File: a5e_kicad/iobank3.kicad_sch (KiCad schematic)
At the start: 3 parts, among them U7 A5EB013B-B23B

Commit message: Add LCSC part numbers and fix C102 footprint
Add a hidden LCSC field to 290 symbols from the JLCPCB parts match
(2026-10-23). Left without LCSC: U7, U15, L1 (not in the JLCPCB
library), C1/C2/C4 and L2-L5 (no value specified), J3 (no confident
match) and Y3 (the 12 pF Basic crystal does not suit the 27 pF load
caps). U2, U12, Y2 and J9 carry the exact-MPN LCSC numbers although
they currently show zero JLCPCB stock.

C102 (22U 6V3) had a 0201 footprint; no 22 uF 0201 part exists. Change
it to 0402 (C415703) like C5-C7.
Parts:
- R23, R248: LCSC (none) -> C25094
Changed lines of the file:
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@@
+			)
+		)
+		(property "LCSC" "C25094"
+			(at 242.57 65.278 90)
+			(hide yes)
+			(show_name no)
+			(do_not_autoplace no)
+			(effects
+				(font
+					(size 1.27 1.27)
+				)
 			)
 		)
@@
 			(at 45.72 124.46 90)
 			(hide yes)
+			(show_name no)
+			(do_not_autoplace no)
+			(effects
+				(font
+					(size 1.27 1.27)
+				)
+			)
+		)
+		(property "LCSC" "C25094"
+			(at 45.72 124.46 90)
+			(hide yes)

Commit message: LPDDR4: connect each DQS pair to its own byte lane
The U7-side DQS labels were crossed (BL0<->BL7, BL1<->BL6): every lane's
DQ/DMI belonged to one memory byte and its strobe to another, which the
Agilex 5 byte swizzle cannot fix. Swap dqs0<->dqs3 and dqs1<->dqs2 on the
bank 3 sheet so BL0/BL1/BL6/BL7 carry A0/A1/B0/B1 complete. The PCB DQS
pairs must be rerouted.
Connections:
- net dqs0_N: now also U7.E62 (3A_B_IO5_IOB_DIFF_IO_3A_B22n); no longer U7.A30 (3A_T_IO89_IOB_DIFF_IO_3A_T4n)
- net dqs0_P: now also U7.G62 (3A_B_IO4_IOB_DIFF_IO_3A_B22p); no longer U7.B28 (3A_T_IO88_IOB_DIFF_IO_3A_T4p)
- net dqs1_N: now also U7.W56 (3A_B_IO17_IOB_DIFF_IO_3A_B16n); no longer U7.E32 (3A_T_IO77_IOB_DIFF_IO_3A_T10n)
- net dqs1_P: now also U7.AB56 (3A_B_IO16_IOB_DIFF_IO_3A_B16p); no longer U7.G32 (3A_T_IO76_IOB_DIFF_IO_3A_T10p)
- net dqs2_N: now also U7.E32 (3A_T_IO77_IOB_DIFF_IO_3A_T10n); no longer U7.W56 (3A_B_IO17_IOB_DIFF_IO_3A_B16n)
- net dqs2_P: now also U7.G32 (3A_T_IO76_IOB_DIFF_IO_3A_T10p); no longer U7.AB56 (3A_B_IO16_IOB_DIFF_IO_3A_B16p)
- net dqs3_N: now also U7.A30 (3A_T_IO89_IOB_DIFF_IO_3A_T4n); no longer U7.E62 (3A_B_IO5_IOB_DIFF_IO_3A_B22n)
- net dqs3_P: now also U7.B28 (3A_T_IO88_IOB_DIFF_IO_3A_T4p); no longer U7.G62 (3A_B_IO4_IOB_DIFF_IO_3A_B22p)
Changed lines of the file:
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@@
 		)
 	)
-	(label "dqs2_N"
+	(label "dqs1_N"
 		(at 208.28 116.84 0)
 		(effects
@@
 		)
 	)
-	(label "dqs1_P"
+	(label "dqs2_P"
 		(at 66.04 88.9 0)
 		(effects
@@
 		)
 	)
-	(label "dqs3_P"
+	(label "dqs0_P"
 		(at 208.28 149.86 0)
 		(effects
@@
 		)
 	)
-	(label "dqs0_N"
+	(label "dqs3_N"
 		(at 66.04 55.88 0)
 		(effects
@@
 		)
 	)
-	(label "dqs0_P"
+	(label "dqs3_P"
 		(at 66.04 58.42 0)
 		(effects
@@
 		)
 	)
-	(label "dqs1_N"
+	(label "dqs2_N"
 		(at 66.04 86.36 0)
 		(effects
@@
 		)
 	)
-	(label "dqs2_P"
+	(label "dqs1_P"
 		(at 208.28 119.38 0)
 		(effects
@@
 		)
 	)
-	(label "dqs3_N"
+	(label "dqs0_N"
 		(at 208.28 147.32 0)
 		(effects

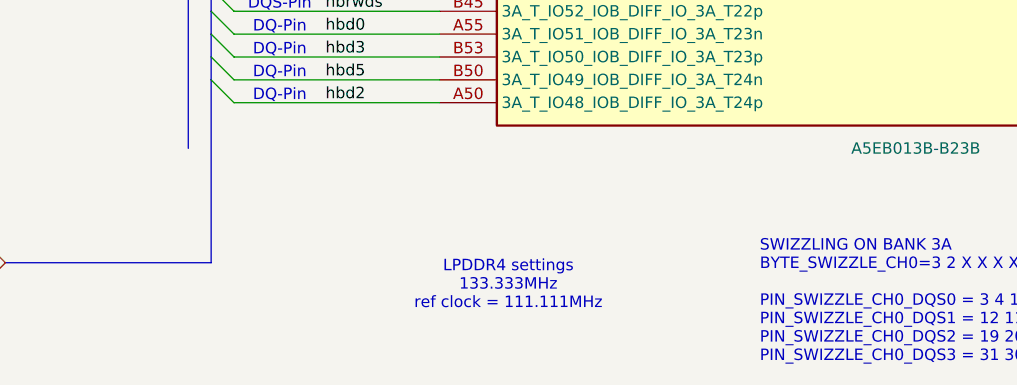
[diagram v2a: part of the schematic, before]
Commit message: L2-L5 1uH (as on the Agilex 3 card), Quartus EMIF/power results recorded
- L2-L5 (3V3/1V8/1V2/1V1 AP61202 bucks) = 1 uH Cenker CKCS201610,
  C97002, the same as on the Agilex 3 card. The AP61202 data sheet asks
  for 1.0-1.5 uH. Per-rail loads from Quartus are 0.2-0.45 A plus board
  loads. The footprint changes from 0805 to 2016.
- Bank 3 note: LPDDR4 1600 MT/s with a 100 MHz U9 refclk, tested in
  Quartus (was the stale 111.111 MHz).
- LPDDR4_SWIZZLE_PLAN.md: both pinout variants pass the fitter;
  swizzle strings, negative control, refclk and refresh-timing notes.
- Checklist: per-rail FPGA power from the Quartus Power Analyzer.
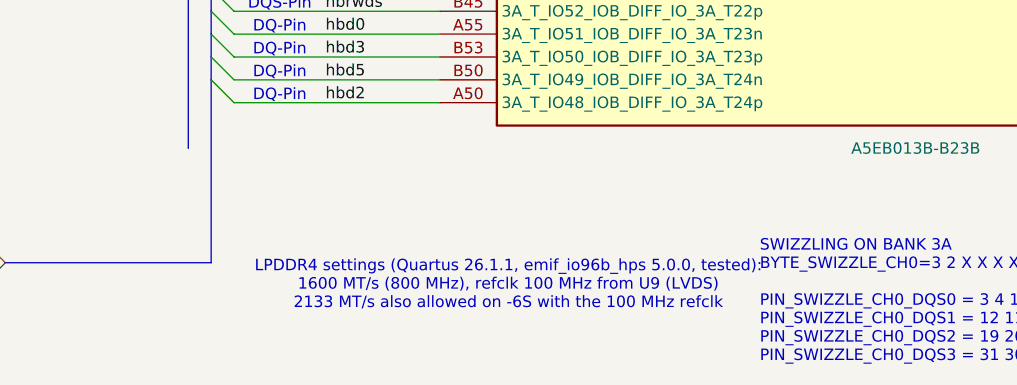
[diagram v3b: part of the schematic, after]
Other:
- note added: "LPDDR4 settings (Quartus 26.1.1, emif_io96b_hps 5.0.0, tested): 1600 MT/s (800 MHz), refclk 100 MHz from U9 (LVDS) 2133 MT/s also allowed on -6S with the 100 MHz refclk"
- note removed: "LPDDR4 settings 133.333MHz ref clock = 111.111MHz"
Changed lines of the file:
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@@
 		)
 	)
-	(text "LPDDR4 settings\n133.333MHz\nref clock = 111.111MHz"
+	(text "LPDDR4 settings (Quartus 26.1.1, emif_io96b_hps 5.0.0, tested):\n1600 MT/s (800 MHz), refclk 100 MHz from U9 (LVDS)\n2133 MT/s also allowed on -6S with the 100 MHz refclk"
 		(exclude_from_sim no)
 		(at 86.36 180.34 0)

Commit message: LPDDR4: variant R pinout (BL6<->BL7, new pin swizzle), strip routing for reroute
- U12 stays at -90 deg on F.Cu (only orientation matching the FPGA lanes;
  0/180 do not fit between board edge and U7, 90 crosses the channels).
- Byte swizzle BL6<->BL7, new pin swizzle in all four lanes, chosen by a
  crossing analysis (straight-line + escape-order model) over rotations,
  positions and all legal swizzles.
- iobank3: 36 U7-side labels permuted; netlist diff only on those U7 pins,
  ERC unchanged (326).
- PCB: all LPDDR4 tracks/arcs/vias and tuning patterns removed, U7 pad nets
  synced; schematic parity 0.
- Quartus 26.1.1 synthesis + fitter pass with the new swizzle strings.
- LPDDR4_SWIZZLE_PLAN.md: research, metric table, lane map, reroute plan.
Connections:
- net dm2: now also U7.A25 (3A_T_IO90_IOB_DIFF_IO_3A_T3p); no longer U7.J27 (3A_T_IO78_IOB_DIFF_IO_3A_T9p)
- net dm3: now also U7.J27 (3A_T_IO78_IOB_DIFF_IO_3A_T9p); no longer U7.A25 (3A_T_IO90_IOB_DIFF_IO_3A_T3p)
- net dq0: now also U7.J65 (3A_B_IO0_IOB_DIFF_IO_3A_B24p); no longer U7.T62 (3A_B_IO2_IOB_DIFF_IO_3A_B23p)
- net dq1: now also U7.G65 (3A_B_IO1_IOB_DIFF_IO_3A_B24n); no longer U7.T56 (3A_B_IO8_IOB_DIFF_IO_3A_B20p)
- net dq10: now also U7.T51 (3A_B_IO22_IOB_DIFF_IO_3A_B13p); no longer U7.M51 (3A_B_IO23_IOB_DIFF_IO_3A_B13n)
- net dq11: now also U7.W48 (3A_B_IO21_IOB_DIFF_IO_3A_B14n); no longer U7.T51 (3A_B_IO22_IOB_DIFF_IO_3A_B13p)
- net dq12: now also U7.M51 (3A_B_IO23_IOB_DIFF_IO_3A_B13n); no longer U7.AB48 (3A_B_IO20_IOB_DIFF_IO_3A_B14p)
- net dq13: now also U7.AB48 (3A_B_IO20_IOB_DIFF_IO_3A_B14p); no longer U7.W48 (3A_B_IO21_IOB_DIFF_IO_3A_B14n)
- net dq14: now also U7.M65 (3A_B_IO15_IOB_DIFF_IO_3A_B17n); no longer U7.T65 (3A_B_IO14_IOB_DIFF_IO_3A_B17p)
- net dq15: now also U7.T65 (3A_B_IO14_IOB_DIFF_IO_3A_B17p); no longer U7.AB62 (3A_B_IO12_IOB_DIFF_IO_3A_B18p)
- net dq16: now also U7.A20 (3A_T_IO95_IOB_DIFF_IO_3A_T1n); no longer U7.G24 (3A_T_IO82_IOB_DIFF_IO_3A_T7p)
- net dq17: now also U7.A22 (3A_T_IO92_IOB_DIFF_IO_3A_T2p); no longer U7.E24 (3A_T_IO83_IOB_DIFF_IO_3A_T7n)
- net dq18: now also U7.A23 (3A_T_IO93_IOB_DIFF_IO_3A_T2n); no longer U7.J35 (3A_T_IO72_IOB_DIFF_IO_3A_T12p)
- net dq19: now also U7.B33 (3A_T_IO84_IOB_DIFF_IO_3A_T6p); no longer U7.T32 (3A_T_IO74_IOB_DIFF_IO_3A_T11p)
- net dq20: now also U7.A33 (3A_T_IO87_IOB_DIFF_IO_3A_T5n); no longer U7.M32 (3A_T_IO75_IOB_DIFF_IO_3A_T11n)
- net dq21: now also U7.A36 (3A_T_IO85_IOB_DIFF_IO_3A_T6n); no longer U7.T24 (3A_T_IO80_IOB_DIFF_IO_3A_T8p)
- net dq22: now also U7.B30 (3A_T_IO86_IOB_DIFF_IO_3A_T5p); no longer U7.G35 (3A_T_IO73_IOB_DIFF_IO_3A_T12n)
- net dq23: now also U7.B22 (3A_T_IO94_IOB_DIFF_IO_3A_T1p); no longer U7.M24 (3A_T_IO81_IOB_DIFF_IO_3A_T8n)
- net dq24: now also U7.M32 (3A_T_IO75_IOB_DIFF_IO_3A_T11n); no longer U7.A22 (3A_T_IO92_IOB_DIFF_IO_3A_T2p)
- net dq25: now also U7.G24 (3A_T_IO82_IOB_DIFF_IO_3A_T7p); no longer U7.A23 (3A_T_IO93_IOB_DIFF_IO_3A_T2n)
- net dq26: now also U7.M24 (3A_T_IO81_IOB_DIFF_IO_3A_T8n); no longer U7.A33 (3A_T_IO87_IOB_DIFF_IO_3A_T5n)
- net dq27: now also U7.T24 (3A_T_IO80_IOB_DIFF_IO_3A_T8p); no longer U7.B33 (3A_T_IO84_IOB_DIFF_IO_3A_T6p)
- net dq28: now also U7.J35 (3A_T_IO72_IOB_DIFF_IO_3A_T12p); no longer U7.B30 (3A_T_IO86_IOB_DIFF_IO_3A_T5p)
- net dq29: now also U7.G35 (3A_T_IO73_IOB_DIFF_IO_3A_T12n); no longer U7.A36 (3A_T_IO85_IOB_DIFF_IO_3A_T6n)
- net dq30: now also U7.T32 (3A_T_IO74_IOB_DIFF_IO_3A_T11p); no longer U7.A20 (3A_T_IO95_IOB_DIFF_IO_3A_T1n)
- net dq31: now also U7.E24 (3A_T_IO83_IOB_DIFF_IO_3A_T7n); no longer U7.B22 (3A_T_IO94_IOB_DIFF_IO_3A_T1p)
- net dq4: now also U7.T56 (3A_B_IO8_IOB_DIFF_IO_3A_B20p); no longer U7.G65 (3A_B_IO1_IOB_DIFF_IO_3A_B24n)
- net dq5: now also U7.M56 (3A_B_IO9_IOB_DIFF_IO_3A_B20n); no longer U7.J65 (3A_B_IO0_IOB_DIFF_IO_3A_B24p)
- net dq6: now also U7.M62 (3A_B_IO3_IOB_DIFF_IO_3A_B23n); no longer U7.M56 (3A_B_IO9_IOB_DIFF_IO_3A_B20n)
- net dq7: now also U7.T62 (3A_B_IO2_IOB_DIFF_IO_3A_B23p); no longer U7.M62 (3A_B_IO3_IOB_DIFF_IO_3A_B23n)
- net dq8: now also U7.AB62 (3A_B_IO12_IOB_DIFF_IO_3A_B18p); no longer U7.W62 (3A_B_IO13_IOB_DIFF_IO_3A_B18n)
- net dq9: now also U7.W62 (3A_B_IO13_IOB_DIFF_IO_3A_B18n); no longer U7.M65 (3A_B_IO15_IOB_DIFF_IO_3A_B17n)
- net dqs2_N: now also U7.A30 (3A_T_IO89_IOB_DIFF_IO_3A_T4n); no longer U7.E32 (3A_T_IO77_IOB_DIFF_IO_3A_T10n)
- net dqs2_P: now also U7.B28 (3A_T_IO88_IOB_DIFF_IO_3A_T4p); no longer U7.G32 (3A_T_IO76_IOB_DIFF_IO_3A_T10p)
- net dqs3_N: now also U7.E32 (3A_T_IO77_IOB_DIFF_IO_3A_T10n); no longer U7.A30 (3A_T_IO89_IOB_DIFF_IO_3A_T4n)
- net dqs3_P: now also U7.G32 (3A_T_IO76_IOB_DIFF_IO_3A_T10p); no longer U7.B28 (3A_T_IO88_IOB_DIFF_IO_3A_T4p)
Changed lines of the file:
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@@
+		)
+	)
+	(label "dm2"
+		(at 66.04 53.34 0)
+		(effects
+			(font
+				(size 1.27 1.27)
+			)
+			(justify left bottom)
 		)
 	)
 	(label "dm3"
-		(at 66.04 53.34 0)
-		(effects
-			(font
-				(size 1.27 1.27)
-			)
-			(justify left bottom)
-		)
-	)
-	(label "dm2"
 		(at 66.04 83.82 0)
 		(effects
@@
 		)
 	)
-	(label "dq14"
+	(label "dq15"
 		(at 208.28 124.46 0)
 		(effects
@@
 		)
 	)
-	(label "dq17"
+	(label "dq31"
 		(at 66.04 71.12 0)
 		(effects
@@
 		)
 	)
-	(label "dq11"
+	(label "dq10"
 		(at 208.28 104.14 0)
 		(effects
@@
 		)
 	)
-	(label "dq15"
+	(label "dq8"
 		(at 208.28 129.54 0)
 		(effects
@@
 		)
 	)
-	(label "dq26"
+	(label "dq20"
 		(at 66.04 60.96 0)
 		(effects
@@
 		)
 	)
-	(label "dq6"
+	(label "dq5"
 		(at 208.28 137.16 0)
 		(effects
@@
 		)
 	)
-	(label "dq12"
+	(label "dq13"
 		(at 208.28 109.22 0)
 		(effects
@@
 		)
 	)
-	(label "dq5"
+	(label "dq0"
 		(at 208.28 160.02 0)
 		(effects
@@
 		)
 	)
-	(label "dq10"
+	(label "dq12"
 		(at 208.28 101.6 0)
 		(effects
@@
 		)
 	)
-	(label "dq0"
+	(label "dq7"
 		(at 208.28 154.94 0)
 		(effects
@@
 		)
 	)
-	(label "dq30"
+	(label "dq16"
 		(at 66.04 40.64 0)
 		(effects
@@
 		)
 	)
-	(label "dq21"
+	(label "dq27"
 		(at 66.04 78.74 0)
 		(effects
@@
 		)
 	)
-	(label "dqs2_P"
+	(label "dqs3_P"
 		(at 66.04 88.9 0)
 		(effects
@@
 		)
 	)
-	(label "dq16"
+	(label "dq25"
 		(at 66.04 73.66 0)
 		(effects
@@
 		)
 	)
-	(label "dq4"
+	(label "dq1"
 		(at 208.28 157.48 0)
 		(effects
@@
 		)
 	)
-	(label "dq19"
+	(label "dq30"
 		(at 66.04 93.98 0)
 		(effects
@@
 		)
 	)
-	(label "dq7"
+	(label "dq6"
 		(at 208.28 152.4 0)
 		(effects
@@
 		)
 	)
-	(label "dq29"
+	(label "dq21"
 		(at 66.04 66.04 0)
 		(effects
@@
 		)
 	)
-	(label "dq18"
+	(label "dq28"
 		(at 66.04 99.06 0)
 		(effects
@@
 		)
 	)
-	(label "dq9"
+	(label "dq14"
 		(at 208.28 121.92 0)
 		(effects
@@
 		)
 	)
-	(label "dqs3_N"
+	(label "dqs2_N"
 		(at 66.04 55.88 0)
 		(effects
@@
 		)
 	)
-	(label "dq31"
+	(label "dq23"
 		(at 66.04 43.18 0)
 		(effects
@@
 		)
 	)
-	(label "dqs3_P"
+	(label "dqs2_P"
 		(at 66.04 58.42 0)
 		(effects
@@
 		)
 	)
-	(label "dq1"
+	(label "dq4"
 		(at 208.28 139.7 0)
 		(effects
@@
 		)
 	)
-	(label "dq23"
+	(label "dq26"
 		(at 66.04 76.2 0)
 		(effects
@@
 		)
 	)
-	(label "dq22"
+	(label "dq29"
 		(at 66.04 96.52 0)
 		(effects
@@
 		)
 	)
-	(label "dq28"
+	(label "dq22"
 		(at 66.04 63.5 0)
 		(effects
@@
 		)
 	)
-	(label "dq27"
+	(label "dq19"
 		(at 66.04 68.58 0)
 		(effects
@@
 		)
 	)
-	(label "dq20"
+	(label "dq24"
 		(at 66.04 91.44 0)
 		(effects
@@
 		)
 	)
-	(label "dqs2_N"
+	(label "dqs3_N"
 		(at 66.04 86.36 0)
 		(effects
@@
 		)
 	)
-	(label "dq13"
+	(label "dq11"
 		(at 208.28 106.68 0)
 		(effects
@@
 		)
 	)
-	(label "dq8"
+	(label "dq9"
 		(at 208.28 127 0)
 		(effects
@@
 		)
 	)
-	(label "dq25"
+	(label "dq18"
 		(at 66.04 45.72 0)
 		(effects
@@
 		)
 	)
-	(label "dq24"
+	(label "dq17"
 		(at 66.04 48.26 0)
 		(effects

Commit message: LPDDR4 variant R2: U12 6 mm left with decaps/fan-out, re-swizzled, planes refilled
- U12 moved from x 165.792 to 159.792 (still F.Cu, -90 deg), centred over
  bank 3A: weighted straight-line crossings -14 %, mean U7->U12 length
  21.2 -> 16.4 mm. -6 mm chosen over -7 mm so the left-end decaps stay
  clear of the 1V1 buck caps (C47/R46) and U9.
- The whole U12 decoupling block moved rigidly with it: 33 B.Cu parts
  (30x 100n under the balls, C48 22u, C69, R44), 111 via-in-pad fan-out
  vias, 36 fan-out tracks. ZQ resistor R43 + its via follow (-5.55 mm).
- Refclk chain R25/R26/C8/C9 moved 1.1 mm down, U9->R->C->U7 B55/A58
  re-routed on B.Cu.
- Planes: removed the 1V8 track on In4 (GND plane) feeding U12 VDD1
  (redundant with the In3 1V8 plane), deleted the dead In6 '1v8' zone,
  refilled all zones with ZONE_FILLER.
- Byte swizzle BL6<->BL7 kept, pin swizzle re-optimised for the new
  position: 19 U7-side labels in iobank3 permuted, U7 pad nets synced.
  Netlist diff only on those pins, ERC unchanged (326), parity 0.
- DRC: 99 violations (was 171; the drop is stale zone fill), 120
  unconnected (unchanged; 64 are the unrouted LPDDR4 nets). LPDDR4
  signals deliberately left unrouted.
- Quartus 26.1.1 synthesis + fitter pass with the new swizzle strings.

NOTE: the board was saved with pcbnew.SaveBoard, which reorders the whole
.kicad_pcb file - the diff is large, but the content changes are only the
ones listed above.
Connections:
- net dq11: now also U7.M51 (3A_B_IO23_IOB_DIFF_IO_3A_B13n); no longer U7.W48 (3A_B_IO21_IOB_DIFF_IO_3A_B14n)
- net dq12: now also U7.W48 (3A_B_IO21_IOB_DIFF_IO_3A_B14n); no longer U7.M51 (3A_B_IO23_IOB_DIFF_IO_3A_B13n)
- net dq15: now also U7.W62 (3A_B_IO13_IOB_DIFF_IO_3A_B18n); no longer U7.T65 (3A_B_IO14_IOB_DIFF_IO_3A_B17p)
- net dq18: now also U7.B30 (3A_T_IO86_IOB_DIFF_IO_3A_T5p); no longer U7.A23 (3A_T_IO93_IOB_DIFF_IO_3A_T2n)
- net dq2: now also U7.M56 (3A_B_IO9_IOB_DIFF_IO_3A_B20n); no longer U7.G56 (3A_B_IO10_IOB_DIFF_IO_3A_B19p)
- net dq20: now also U7.A36 (3A_T_IO85_IOB_DIFF_IO_3A_T6n); no longer U7.A33 (3A_T_IO87_IOB_DIFF_IO_3A_T5n)
- net dq21: now also U7.A33 (3A_T_IO87_IOB_DIFF_IO_3A_T5n); no longer U7.A36 (3A_T_IO85_IOB_DIFF_IO_3A_T6n)
- net dq22: now also U7.B22 (3A_T_IO94_IOB_DIFF_IO_3A_T1p); no longer U7.B30 (3A_T_IO86_IOB_DIFF_IO_3A_T5p)
- net dq23: now also U7.A23 (3A_T_IO93_IOB_DIFF_IO_3A_T2n); no longer U7.B22 (3A_T_IO94_IOB_DIFF_IO_3A_T1p)
- net dq24: now also U7.G24 (3A_T_IO82_IOB_DIFF_IO_3A_T7p); no longer U7.M32 (3A_T_IO75_IOB_DIFF_IO_3A_T11n)
- net dq25: now also U7.T24 (3A_T_IO80_IOB_DIFF_IO_3A_T8p); no longer U7.G24 (3A_T_IO82_IOB_DIFF_IO_3A_T7p)
- net dq26: now also U7.M32 (3A_T_IO75_IOB_DIFF_IO_3A_T11n); no longer U7.M24 (3A_T_IO81_IOB_DIFF_IO_3A_T8n)
- net dq27: now also U7.J35 (3A_T_IO72_IOB_DIFF_IO_3A_T12p); no longer U7.T24 (3A_T_IO80_IOB_DIFF_IO_3A_T8p)
- net dq28: now also U7.G35 (3A_T_IO73_IOB_DIFF_IO_3A_T12n); no longer U7.J35 (3A_T_IO72_IOB_DIFF_IO_3A_T12p)
- net dq29: now also U7.T32 (3A_T_IO74_IOB_DIFF_IO_3A_T11p); no longer U7.G35 (3A_T_IO73_IOB_DIFF_IO_3A_T12n)
- net dq30: now also U7.M24 (3A_T_IO81_IOB_DIFF_IO_3A_T8n); no longer U7.T32 (3A_T_IO74_IOB_DIFF_IO_3A_T11p)
- net dq4: now also U7.G56 (3A_B_IO10_IOB_DIFF_IO_3A_B19p); no longer U7.T56 (3A_B_IO8_IOB_DIFF_IO_3A_B20p)
- net dq5: now also U7.T56 (3A_B_IO8_IOB_DIFF_IO_3A_B20p); no longer U7.M56 (3A_B_IO9_IOB_DIFF_IO_3A_B20n)
- net dq9: now also U7.T65 (3A_B_IO14_IOB_DIFF_IO_3A_B17p); no longer U7.W62 (3A_B_IO13_IOB_DIFF_IO_3A_B18n)
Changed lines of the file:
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@@
 		)
 	)
-	(label "dq15"
+	(label "dq9"
 		(at 208.28 124.46 0)
 		(effects
@@
 		)
 	)
-	(label "dq20"
+	(label "dq21"
 		(at 66.04 60.96 0)
 		(effects
@@
 		)
 	)
-	(label "dq5"
+	(label "dq2"
 		(at 208.28 137.16 0)
 		(effects
@@
 		)
 	)
-	(label "dq12"
+	(label "dq11"
 		(at 208.28 101.6 0)
 		(effects
@@
 		)
 	)
-	(label "dq27"
+	(label "dq25"
 		(at 66.04 78.74 0)
 		(effects
@@
 		)
 	)
-	(label "dq25"
+	(label "dq24"
 		(at 66.04 73.66 0)
 		(effects
@@
 		)
 	)
-	(label "dq30"
+	(label "dq29"
 		(at 66.04 93.98 0)
 		(effects
@@
 		)
 	)
-	(label "dq21"
+	(label "dq20"
 		(at 66.04 66.04 0)
 		(effects
@@
 		)
 	)
-	(label "dq28"
+	(label "dq27"
 		(at 66.04 99.06 0)
 		(effects
@@
 		)
 	)
-	(label "dq23"
+	(label "dq22"
 		(at 66.04 43.18 0)
 		(effects
@@
 		)
 	)
-	(label "dq4"
+	(label "dq5"
 		(at 208.28 139.7 0)
 		(effects
@@
 		)
 	)
-	(label "dq26"
+	(label "dq30"
 		(at 66.04 76.2 0)
 		(effects
@@
 		)
 	)
-	(label "dq29"
+	(label "dq28"
 		(at 66.04 96.52 0)
 		(effects
@@
 		)
 	)
-	(label "dq22"
+	(label "dq18"
 		(at 66.04 63.5 0)
 		(effects
@@
 		)
 	)
-	(label "dq24"
+	(label "dq26"
 		(at 66.04 91.44 0)
 		(effects
@@
 		)
 	)
-	(label "dq2"
+	(label "dq4"
 		(at 208.28 134.62 0)
 		(effects
@@
 		)
 	)
-	(label "dq11"
+	(label "dq12"
 		(at 208.28 106.68 0)
 		(effects
@@
 		)
 	)
-	(label "dq9"
+	(label "dq15"
 		(at 208.28 127 0)
 		(effects
@@
 		)
 	)
-	(label "dq18"
+	(label "dq23"
 		(at 66.04 45.72 0)
 		(effects
